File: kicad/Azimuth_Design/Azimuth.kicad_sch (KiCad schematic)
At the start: 20 parts, among them IC1 BNO086, U1 ESP32-C3-WROOM-02-N4(4MB)

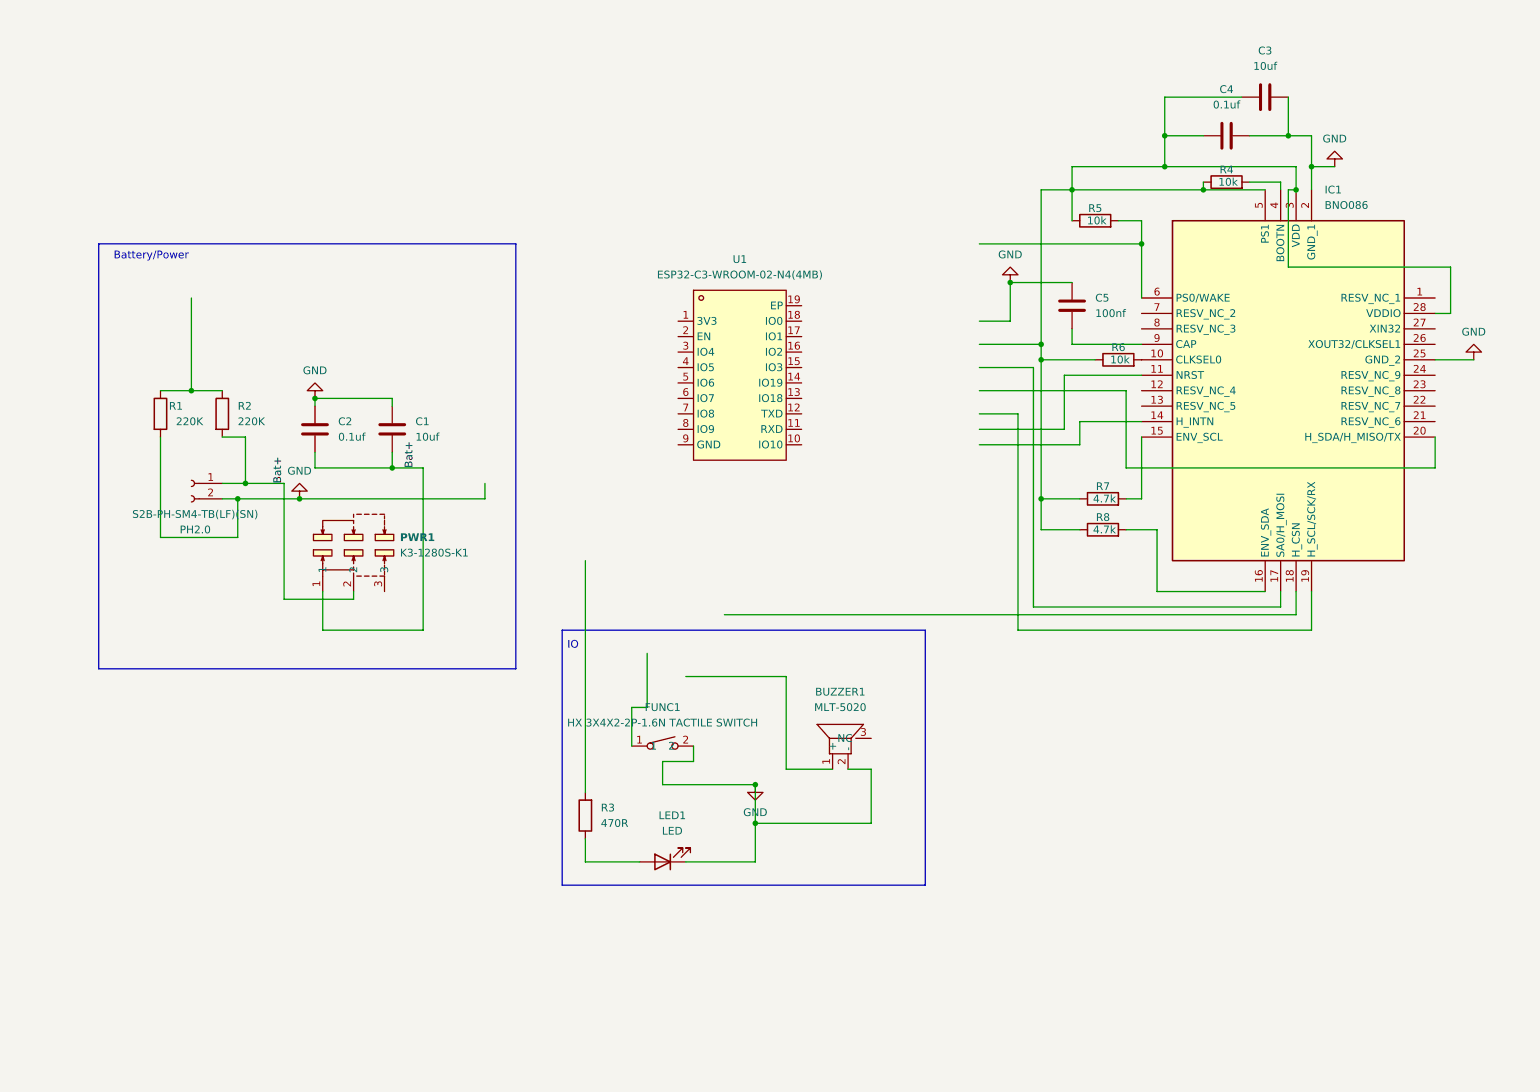
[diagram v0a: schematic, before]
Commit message: new offical azimuth PCB design started, big doc updates
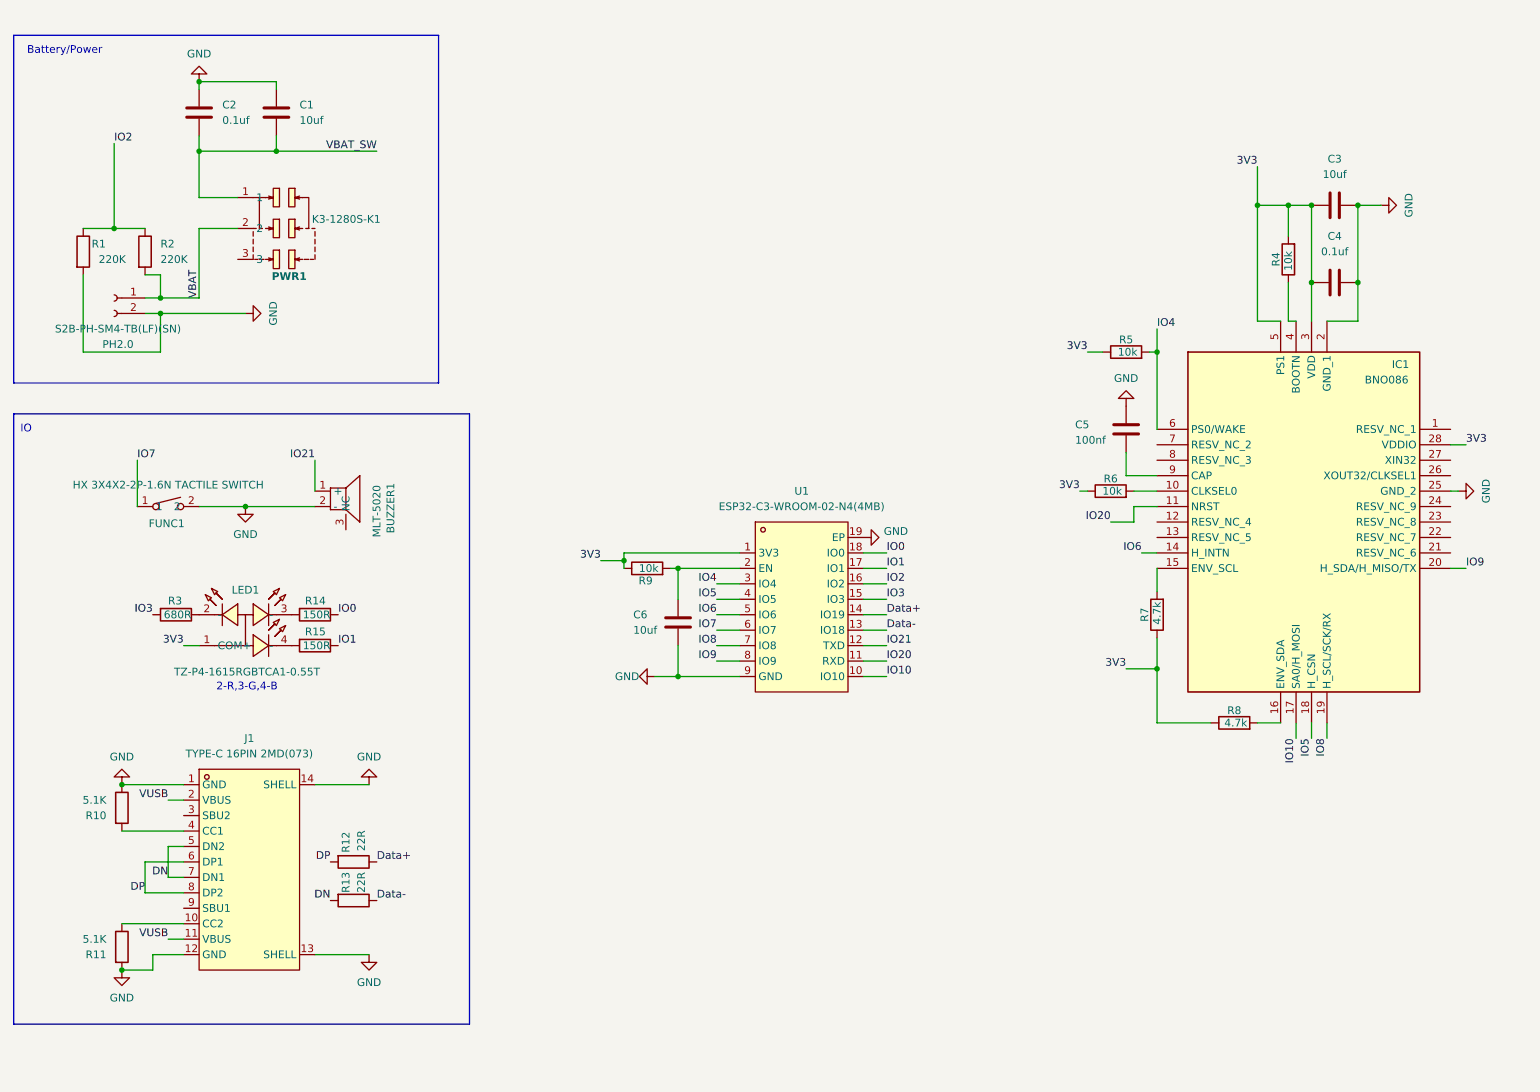
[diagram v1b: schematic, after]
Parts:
- removed LED1: LED, LED_SMD:LED_0402_1005Metric, symbol Device:LED
- added C6: 10uf, Capacitor_SMD:C_0603_1608Metric, symbol Device:C
- added J1: TYPE-C 16PIN 2MD(073), usb_type_c_C2765186:USB-C-SMD_TYPE-C-6PIN-2MD-073, symbol 1_MyLib:TYPE-C16PIN2MD(073)
- added LED1: TZ-P4-1615RGBTCA1-0.55T, rgb_led_C779813:LED-SMD_4P-L1.6-W1.5-BR_TZ-P4-1615, symbol 1_MyLib:TZ-P4-1615RGBTCA1-0.55T
- added R10, R11: 5.1K, Resistor_SMD:R_0402_1005Metric, symbol Device:R
- added R12, R13: 22R, Resistor_SMD:R_0402_1005Metric, symbol Device:R
- added R14, R15: 150R, Resistor_SMD:R_0402_1005Metric, symbol Device:R
- added R9: 10k, Resistor_SMD:R_0402_1005Metric, symbol Device:R
- R3: value 470R -> 680R; LCSC Part C114877 -> (none); Manufacturer_Part_Number RC0402FR-07470RL -> (none)
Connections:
- net GND: now also U1.19 (EP), U1.9 (GND), C6.1, J1.1 (GND), J1.12 (GND), J1.13 (SHELL), J1.14 (SHELL), R10.1, R11.2
- net IO2: now reaches R1.1, R2.1
- net IO2: now also U1.16 (IO2)
- net 3V3: now reaches U1.1 (3V3)
- net 3V3: now also C3.2, C4.2, IC1.28 (VDDIO), IC1.3 (VDD), IC1.5 (PS1), R4.2, R5.1, R6.1, R7.1, R8.1, LED1.1 (COM+), R9.1
- net IO10: now reaches U1.10 (IO10)
- net IO10: now also IC1.17 (SA0/H_MOSI)
- net IO20: now reaches U1.11 (RXD)
- net IO20: now also IC1.11 (NRST)
- net IO21: now reaches U1.12 (TXD)
- net IO21: now also BUZZER1.1 (+)
- net Data-: now reaches U1.13 (IO18)
- net Data-: now also R13.1
- net Data+: now reaches U1.14 (IO19)
- net Data+: now also R12.1
- net IO3: now reaches U1.15 (IO3)
- net IO3: now also R3.2
- net IO1: now reaches U1.17 (IO1)
- net IO1: now also R15.1
- net IO0: now reaches U1.18 (IO0)
- net IO0: now also R14.1
- net at U1.2 (EN): now also C6.2, R9.2
- net IO4: now reaches U1.3 (IO4)
- net IO4: now also IC1.6 (PS0/WAKE), R5.2
- net IO5: now reaches U1.4 (IO5)
- net IO5: now also IC1.18 (H_CSN)
- net IO6: now reaches U1.5 (IO6)
- net IO6: now also IC1.14 (H_INTN)
- net IO7: now reaches U1.6 (IO7)
- net IO7: now also FUNC1.1
- net IO8: now reaches U1.7 (IO8)
- net IO8: now also IC1.19 (H_SCL/SCK/RX)
- net IO9: now reaches U1.8 (IO9)
- net IO9: now also IC1.20 (H_SDA/H_MISO/TX)
- net at R3.1: now also LED1.2 (-)
- net at IC1.4 (BOOTN): now also R4.1; no longer R4.2
- net Bat+ renamed VBAT
- net VBAT: no longer C1.2, C2.1, PWR1.1
- new net: J1.10 (CC2), R11.1
- new net: J1.4 (CC1), R10.2
- new net: LED1.4 (-), R15.2
- new net: LED1.3 (-), R14.2
- new net DN: J1.5 (DN2), J1.7 (DN1), R13.2
- new net DP: J1.6 (DP1), J1.8 (DP2), R12.2
- new net VBAT_SW: C1.2, C2.1, PWR1.1
- new net VUSB: J1.11 (VBUS), J1.2 (VBUS)
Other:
- note added: "2-R,3-G,4-B"
- moved on the sheet: BUZZER1, C1, C2, C3, C4, C5, FUNC1, IC1, PH2.0, PWR1, R1, R2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

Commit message: schematic fixes
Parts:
- C6: value 10uf -> 1uf; LCSC Part C19702 -> (none); Manufacturer_Part_Number CL10A106KP8NNNC -> (none)
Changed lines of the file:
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@@
 			)
 		)
-		(property "Value" "10uf"
+		(property "Value" "1uf"
 			(at 125.984 120.65 0)
 			(effects
@@
 			)
 		)
-		(property "Manufacturer_Part_Number" "CL10A106KP8NNNC"
+		(property "Manufacturer_Part_Number" ""
 			(at 133.35 119.38 0)
 			(effects
@@
 			)
 		)
-		(property "LCSC Part" "C19702"
+		(property "LCSC Part" ""
 			(at 133.35 119.38 0)
 			(effects

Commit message: big docs refinement
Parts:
- C3: renamed from C6; value 1uf -> 100nf
- renumbered C3 to C4, C4 to C5, C5 to C6, R9 to R10, R4 to R11, R5 to R12, R6 to R13, R7 to R14, R8 to R15, R14 to R4, R15 to R5, R10 to R6, R11 to R7, R12 to R8, R13 to R9
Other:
- moved on the sheet: BUZZER1, FUNC1, J1, LED1, R3, R4, R5, R6, R7, R8, R9
